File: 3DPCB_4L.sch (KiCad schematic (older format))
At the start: 186 parts, among them IC1 DRV8825, IC2 DRV8825, IC3 DRV8825, IC4 DRV8825, IC5 DRV8825, IC6 MP9943, J10 , J11 , J12 , J13 , J14 , J15 , J16 , J2 , J3 , J4 , J5 , J6 , J7 , J8 , J9 , K1 CONN_3, K2 CONN_3, K3 CONN_3, K4 CONN_3, K5 CONN_3, K6 CONN_3, K7 CONN_3, K8 CONN_3, K9 CONN_3, P1 CONN_8, P11 CONN_3X2, P12 CONN_3X2, P13 CONN_4, P2 CONN_8, P5 CONN_4, P6 CONN_4, P7 CONN_4, P8 CONN_02X03, P9 CONN_4, U1 CONN_4_LERCHE, U10 MICRO-SD, U11 TC4427, U12 MCP4728, U13 CONN_4_LERCHE, U15 SPST_MOMENTARY, U16 CONN_4_LERCHE, U2 SPST_MOMENTARY, U21 CONN_4_LERCHE, U22 CONN_4_LERCHE, U23 MCP4728, U24 IRFH5302, U25 CONN_4_LERCHE, U3 BSS84, U4 CONN_4_LERCHE, U5 IRFH5302, U6 LPC1768_TQFP100, U7 IRFH5302, U8 IRFH5302, U9 TC4427

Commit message: Minor changes DONT USE NOW
Do not use this right now, changes are still coming in.
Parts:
- L2: value IHLP1212-10uH -> IHLP1212BZER2R2M11
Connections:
- net labels added: P2.11
- net labels removed: SD_CD
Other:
- note added: "Filter-caps placed closely to LPC1769"
- note added: "Todo: Change so external Ethernet-board is \npossible to add. 18-11-2016"
- moved on the sheet: C49, D10, R17, R41, R42, R43, U10

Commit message: Branching to follow Smoothieboard V1.1
Update, following Smoothieboard V1.1
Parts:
- added U?: A5984_LP, symbol A5984_LP
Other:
- moved on the sheet: C22, C23, C24, C25, C26, C27, C28, C29, C30, C31, C70, C71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

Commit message: Added A5984 to schematic
Added A5984 to schematic
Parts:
- removed C35, C40, C41, C42, C68: 470n, LercheTech:Lerche_C0603, symbol C-RESCUE-3DPCB_4L
- removed IC1, IC2, IC3, IC4, IC5: DRV8825, LercheTech:Lerche_TSSOP28_EP, symbol DRV8825
- added IC1, IC2, IC3, IC4: A5984_LP, LercheTech:Lerche_TSSOP24_EP, symbol A5984_LP
- C36, C37, C8: value 10n -> 100nF
- C67: value 10n -> 100n
- IC5: renamed from U?; footprint (none) -> LercheTech:Lerche_TSSOP24_EP
- R21, R22, R23, R24, R29, R30, R31, R32, R33, R37: value 0R1 -> 0R05
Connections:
- net labels removed: ~FAULT1, ~FAULT2, ~FAULT3, ~FAULT4, ~FAULT5, ~HOME1, ~HOME2, ~HOME3, ~HOME4, ~HOME5
- wire segments 446 -> 477
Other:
- moved on the sheet: C22, C23, C24, C25, C26, C27, C28, C29, C30, C31, C32, C33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

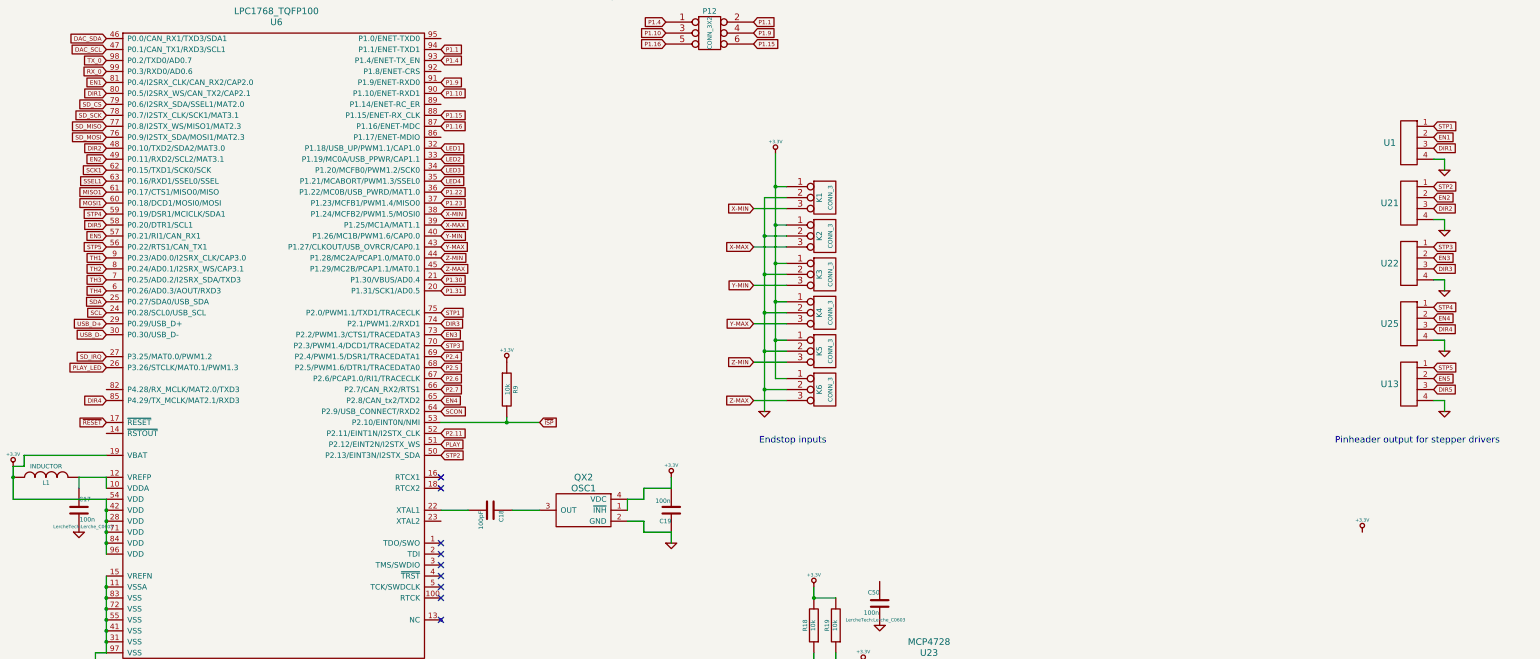
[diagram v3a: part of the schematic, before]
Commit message: First A5984 in place - DO NOT USE
First A5984 in place - DO NOT USE
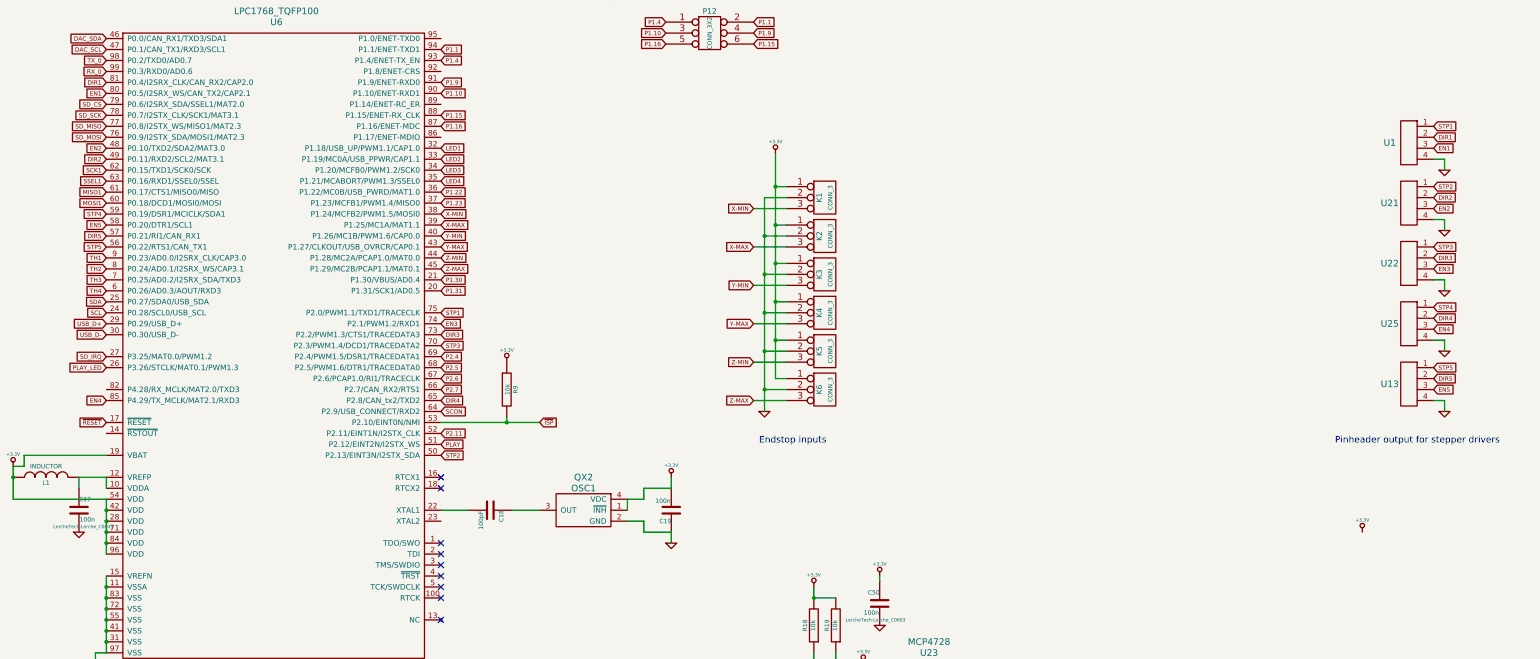
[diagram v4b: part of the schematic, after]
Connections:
- net +3.3V: now also C50.1
- net DIR1: now also U1.2, U6.81 (P0.4/I2SRX_CLK/CAN_RX2/CAP2.0); no longer U1.3, U6.80 (P0.5/I2SRX_WS/CAN_TX2/CAP2.1)
- net DIR2: now also U21.2, U6.49 (P0.11/RXD2/SCL2/MAT3.1); no longer U21.3, U6.48 (P0.10/TXD2/SDA2/MAT3.0)
- net DIR3: now also U22.2, U6.73 (P2.2/PWM1.3/CTS1/TRACEDATA3); no longer U22.3, U6.74 (P2.1/PWM1.2/RXD1)
- net DIR4: now also U25.2, U6.65 (P2.8/CAN_tx2/TXD2); no longer U25.3, U6.85 (P4.29/TX_MCLK/MAT2.1/RXD3)
- net DIR5: now also U13.2, U6.57 (P0.21/RI1/CAN_RX1); no longer U13.3, U6.58 (P0.20/DTR1/SCL1)
- net EN1: now also U1.3, U6.80 (P0.5/I2SRX_WS/CAN_TX2/CAP2.1); no longer U1.2, U6.81 (P0.4/I2SRX_CLK/CAN_RX2/CAP2.0)
- net EN2: now also U21.3, U6.48 (P0.10/TXD2/SDA2/MAT3.0); no longer U21.2, U6.49 (P0.11/RXD2/SCL2/MAT3.1)
- net EN3: now also U22.3, U6.74 (P2.1/PWM1.2/RXD1); no longer U22.2, U6.73 (P2.2/PWM1.3/CTS1/TRACEDATA3)
- net EN4: now also U25.3, U6.85 (P4.29/TX_MCLK/MAT2.1/RXD3); no longer U25.2, U6.65 (P2.8/CAN_tx2/TXD2)
- net EN5: now also U13.3, U6.58 (P0.20/DTR1/SCL1); no longer U13.2, U6.57 (P0.21/RI1/CAN_RX1)

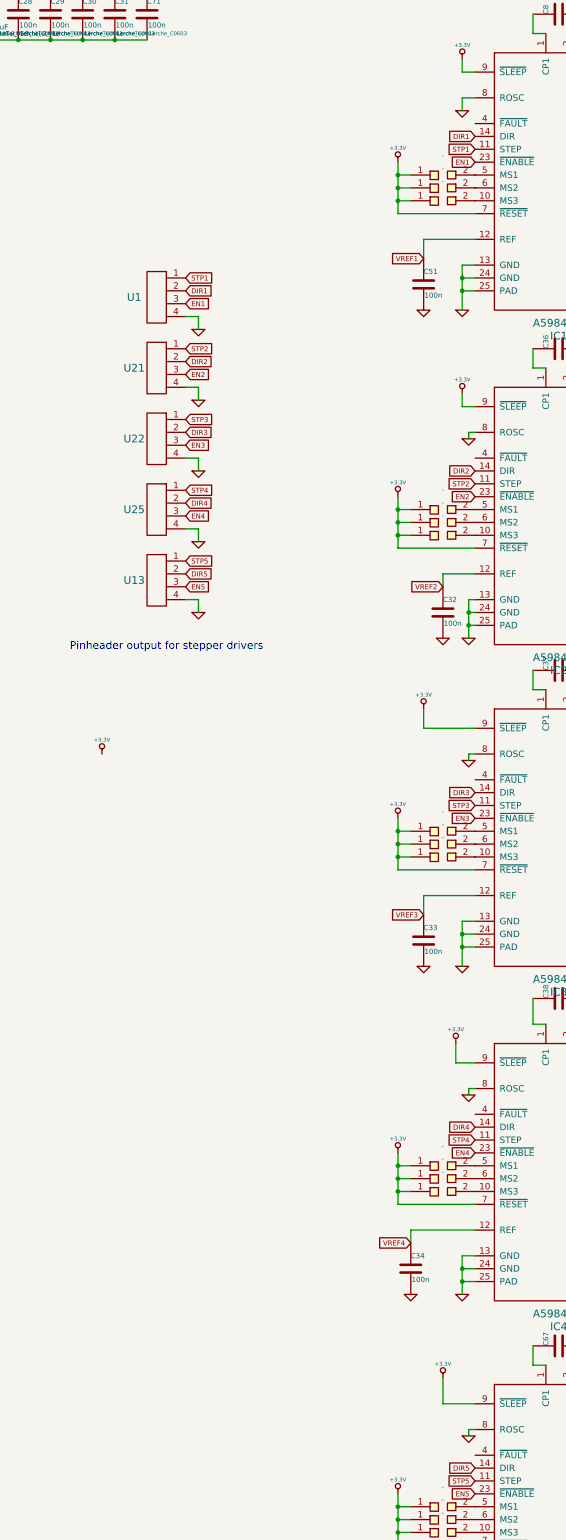
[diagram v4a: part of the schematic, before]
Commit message: Adding resistor to ROSC - DONT USE
DONT USE YET
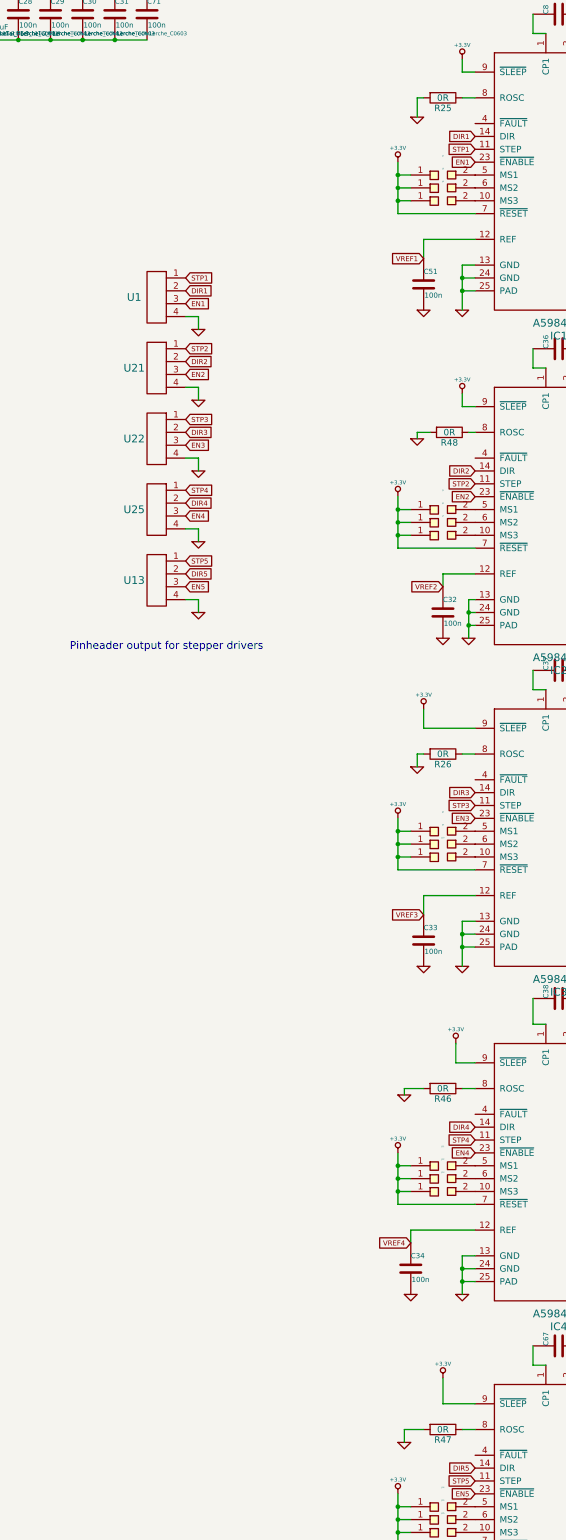
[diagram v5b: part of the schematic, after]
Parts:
- added R25, R26, R46, R47, R48: 0R, LercheTech:Lerche_R0603, symbol R
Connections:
- net GND: now also R25.2, R26.2, R46.2, R47.2, R48.2; no longer IC1.8 (ROSC), IC2.8 (ROSC), IC3.8 (ROSC), IC4.8 (ROSC), IC5.8 (ROSC)
- new net: IC5.8 (ROSC), R47.1
- new net: IC4.8 (ROSC), R46.1
- new net: IC3.8 (ROSC), R26.1
- new net: IC2.8 (ROSC), R48.1
- new net: IC1.8 (ROSC), R25.1

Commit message: Added smaller parts
Added LEDs to MOSFETs, adding AVCC and AGND connector
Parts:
- added C35: 100n, LercheTech:Lerche_C0603, symbol C-RESCUE-3DPCB_4L
- added D11, D12, D13, D14: LED, LEDs:LED_0603, symbol LED-RESCUE-3DPCB_4L
- added P3: CONN_01X02, Pin_Headers:Pin_Header_Straight_1x02_Pitch2.54mm, symbol CONN_01X02
- added R49, R50, R51, R52: 4k7, LercheTech:Lerche_R0603, symbol R-RESCUE-3DPCB_4L
- P8: footprint (none) -> LercheTech:Lerche_Molex_Microfit_0430450607
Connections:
- net GND: now also C35.2, D11.2 (K), D12.2 (K), D13.2 (K), D14.2 (K), P3.2 (P2)
- net at C17.1, L1.2, U6.10 (VDDA)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: now also C35.1, P3.1 (P1)
- net at R14.1, R56.2, U5.1 (G): now also R49.1
- net at R15.1, R58.2, U7.1 (G): now also R50.1
- net at R16.1, R57.2, U8.1 (G): now also R51.1
- net at R20.1, R59.2, U24.1 (G): now also R52.1
- new net: D13.1 (A), R49.2
- new net: D14.1 (A), R51.2
- new net: D11.1 (A), R50.2
- new net: D12.1 (A), R52.2
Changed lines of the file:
@@
 F 0 "C17" H 5450 6800 40  0000 L CNN
 F 1 "100n" H 5456 6615 40  0000 L CNN
-F 2 "LercheTech:Lerche_C0603" H 5488 6550 30  0000 C CNN
+F 2 "LercheTech:Lerche_C0603" H 5488 6550 30  0001 C CNN
 F 3 "~" H 5450 6700 60  0000 C CNN
 	1    5450 6700
@@
 Connection ~ 4850 6400
 Wire Wire Line
-	5450 6400 5450 6500
+	5450 5900 5450 6500
 Wire Wire Line
 	3400 1850 4300 1850
@@
 	10950 11050 11150 11050
 Wire Wire Line
-	11050 11150 11050 11050
+	11050 10500 11050 11150
 Connection ~ 11050 11050
 Wire Wire Line
@@
 	13600 11050 13800 11050
 Wire Wire Line
-	13700 11150 13700 11050
+	13700 10450 13700 11150
 Connection ~ 13700 11050
 Wire Wire Line
 	13600 12300 13800 12300
 Wire Wire Line
-	13700 12400 13700 12300
+	13700 11950 13700 12400
 Connection ~ 13700 12300
 Wire Wire Line
-	11050 12400 11050 12300
+	11050 11950 11050 12400
 Wire Wire Line
 	10950 12300 11150 12300
@@
 Text Notes 12200 9750 0    60   ~ 0
 DAC's for stepper current control
-Text Notes 11250 10450 0    60   ~ 0
+Text Notes 11200 10150 0    60   ~ 0
 MOSFET outputs
 Text Notes 4100 10500 0    60   ~ 0
@@
 $EndComp
 Wire Wire Line
-	9850 11200 10700 11200
+	9850 11450 9850 11750
 Wire Wire Line
-	10700 11200 10700 11750
-Wire Wire Line
-	10700 11750 13000 11750
+	9850 11750 13000 11750
 Wire Wire Line
 	13000 11750 13000 11050
 Wire Wire Line
-	9850 12450 10250 12450
-Wire Wire Line
-	10250 12450 10250 13150
+	9850 12750 9850 13150
 Wire Wire Line
-	10250 13150 13000 13150
+	9850 13150 13000 13150
 Wire Wire Line
 	13000 13150 13000 12300
@@
 Wire Wire Line
 	9850 11050 9850 10650
-Wire Wire Line
-	9850 10650 9550 10650
-Wire Wire Line
-	9850 11200 9850 11450
-Wire Wire Line
-	9850 11450 9550 11450
 $Comp
 L C C49
@@
 $EndComp
 Wire Wire Line
-	9850 12450 9850 12750
-Wire Wire Line
-	9850 12750 9550 12750
-Wire Wire Line
 	9850 12300 9850 12000
-Wire Wire Line
-	9850 12000 9550 12000
 Text GLabel 9050 9650 0    39   Input ~ 0
 MOSVCC
@@
 F 0 "P8" H 1400 4500 50  0000 C CNN
 F 1 "CONN_02X03" H 1400 4100 50  0000 C CNN
-F 2 "" H 1400 3100 50  0000 C CNN
+F 2 "LercheTech:Lerche_Molex_Microfit_0430450607" H 1400 3100 50  0001 C CNN
 F 3 "" H 1400 3100 50  0000 C CNN
 	1    1400 4300
@@
 $EndComp
 Wire Wire Line
-	20050 3300 19950 3300
+	19950 3300 20050 3300
 Wire Wire Line
 	19950 3100 19950 3450
@@
 $EndComp
 Wire Wire Line
-	20050 2700 19450 2700
+	19450 2700 20050 2700
 Wire Wire Line
-	19450 2700 19450 2300
+	19450 2300 19450 2700
 Wire Wire Line
 	19550 2600 19450 2600
@@
 Wire Wire Line
 	19500 12150 19500 12250
+$Comp
+L CONN_01X02 P3
+U 1 1 58779D11
+P 4300 5950
+F 0 "P3" H 4300 6100 50  0000 C CNN
+F 1 "CONN_01X02" V 4400 5950 50  0000 C CNN
+F 2 "Pin_Headers:Pin_Header_Straight_1x02_Pitch2.54mm" H 4300 5950 50  0001 C CNN
+F 3 "" H 4300 5950 50  0000 C CNN
+	1    4300 5950
+	-1   0    0    -1
+$EndComp
+Connection ~ 5450 6400
+Wire Wire Line
+	5450 5900 4500 5900
+$Comp
+L GND-RESCUE-3DPCB_4L #PWR0131
+U 1 1 5877C07D
+P 4600 6100
+F 0 "#PWR0131" H 4600 6100 30  0001 C CNN
+F 1 "GND" H 4600 6030 30  0001 C CNN
+F 2 "" H 4600 6100 60  0000 C CNN
+F 3 "" H 4600 6100 60  0000 C CNN
+	1    4600 6100
+	1    0    0    -1
+$EndComp
+Wire Wire Line
+	4500 6000 4600 6000
+Wire Wire Line
+	4600 5750 4600 6100
+$Comp
+L R-RESCUE-3DPCB_4L R49
+U 1 1 5879127B
+P 11300 10500
+F 0 "R49" V 11380 10500 40  0000 C CNN
+F 1 "4k7" V 11307 10501 40  0000 C CNN
+F 2 "LercheTech:Lerche_R0603" V 11230 10500 30  0001 C CNN
+F 3 "~" H 11300 10500 30  0000 C CNN
+	1    11300 10500
+	0    -1   -1   0
+$EndComp
+$Comp
+L LED-RESCUE-3DPCB_4L D13
+U 1 1 587971F1
+P 11850 10500
+F 0 "D13" H 11850 10600 50  0000 C CNN
+F 1 "LED" H 11850 10400 50  0000 C CNN
+F 2 "LEDs:LED_0603" H 11850 10500 60  0001 C CNN
+F 3 "~" H 11850 10500 60  0000 C CNN
+	1    11850 10500
+	1    0    0    -1
+$EndComp
+Wire Wire Line
+	11650 10500 11550 10500
+$Comp
+L GND-RESCUE-3DPCB_4L #PWR0132
+U 1 1 5879B521
+P 12050 10500
+F 0 "#PWR0132" H 12050 10500 30  0001 C CNN
+F 1 "GND" H 12050 10430 30  0001 C CNN
+F 2 "" H 12050 10500 60  0000 C CNN
+F 3 "" H 12050 10500 60  0000 C CNN
+	1    12050 10500
+	0    -1   -1   0
+$EndComp
+$Comp
+L R-RESCUE-3DPCB_4L R51
+U 1 1 5879B769
+P 11300 11950
+F 0 "R51" V 11380 11950 40  0000 C CNN
+F 1 "4k7" V 11307 11951 40  0000 C CNN
+F 2 "LercheTech:Lerche_R0603" V 11230 11950 30  0001 C CNN
+F 3 "~" H 11300 11950 30  0000 C CNN
+	1    11300 11950
+	0    -1   -1   0
+$EndComp
+$Comp
+L LED-RESCUE-3DPCB_4L D14
+U 1 1 5879BFF3
+P 11850 11950
+F 0 "D14" H 11850 12050 50  0000 C CNN
+F 1 "LED" H 11850 11850 50  0000 C CNN
+F 2 "LEDs:LED_0603" H 11850 11950 60  0001 C CNN
+F 3 "~" H 11850 11950 60  0000 C CNN
+	1    11850 11950
+	1    0    0    -1
+$EndComp
+$Comp
+L GND-RESCUE-3DPCB_4L #PWR0133
+U 1 1 5879C507
+P 12050 11950
+F 0 "#PWR0133" H 12050 11950 30  0001 C CNN
+F 1 "GND" H 12050 11880 30  0001 C CNN
+F 2 "" H 12050 11950 60  0000 C CNN
+F 3 "" H 12050 11950 60  0000 C CNN
+	1    12050 11950
+	0    -1   -1   0
+$EndComp
+Wire Wire Line
+	11650 11950 11550 11950
+$Comp
+L R-RESCUE-3DPCB_4L R50
+U 1 1 5879F744
+P 13950 10450
+F 0 "R50" V 14030 10450 40  0000 C CNN
+F 1 "4k7" V 13957 10451 40  0000 C CNN
+F 2 "LercheTech:Lerche_R0603" V 13880 10450 30  0001 C CNN
+F 3 "~" H 13950 10450 30  0000 C CNN
+	1    13950 10450
+	0    -1   -1   0
+$EndComp
+$Comp
+L LED-RESCUE-3DPCB_4L D11
+U 1 1 5879F9AC
+P 14400 10450
+F 0 "D11" H 14400 10550 50  0000 C CNN
+F 1 "LED" H 14400 10350 50  0000 C CNN
+F 2 "LEDs:LED_0603" H 14400 10450 60  0001 C CNN
+F 3 "~" H 14400 10450 60  0000 C CNN
+	1    14400 10450
+	1    0    0    -1
+$EndComp
+$Comp
+L GND-RESCUE-3DPCB_4L #PWR0134
+U 1 1 5879FC1F
+P 14650 10550
+F 0 "#PWR0134" H 14650 10550 30  0001 C CNN
+F 1 "GND" H 14650 10480 30  0001 C CNN
+F 2 "" H 14650 10550 60  0000 C CNN
+F 3 "" H 14650 10550 60  0000 C CNN
+	1    14650 10550
+	1    0    0    -1
+$EndComp
+Wire Wire Line
+	14600 10450 14650 10450
+Wire Wire Line
+	14650 10450 14650 10550
+$Comp
+L R-RESCUE-3DPCB_4L R52
+U 1 1 587A1BB4
+P 13950 11950
+F 0 "R52" V 14030 11950 40  0000 C CNN
+F 1 "4k7" V 13957 11951 40  0000 C CNN
+F 2 "LercheTech:Lerche_R0603" V 13880 11950 30  0001 C CNN
+F 3 "~" H 13950 11950 30  0000 C CNN
+	1    13950 11950
+	0    -1   -1   0
+$EndComp
+$Comp
+L LED-RESCUE-3DPCB_4L D12
+U 1 1 587A1E30
+P 14400 11950
+F 0 "D12" H 14400 12050 50  0000 C CNN
+F 1 "LED" H 14400 11850 50  0000 C CNN
+F 2 "LEDs:LED_0603" H 14400 11950 60  0001 C CNN
+F 3 "~" H 14400 11950 60  0000 C CNN
+	1    14400 11950
+	1    0    0    -1
+$EndComp
+$Comp
+L GND-RESCUE-3DPCB_4L #PWR0135
+U 1 1 587A20AD
+P 14650 12050
+F 0 "#PWR0135" H 14650 12050 30  0001 C CNN
+F 1 "GND" H 14650 11980 30  0001 C CNN
+F 2 "" H 14650 12050 60  0000 C CNN
+F 3 "" H 14650 12050 60  0000 C CNN
+	1    14650 12050
+	1    0    0    -1
+$EndComp
+Wire Wire Line
+	14600 11950 14650 11950
+Wire Wire Line
+	14650 11950 14650 12050
+Wire Wire Line
+	9850 10650 9550 10650
+Wire Wire Line
+	9850 12750 9550 12750
+Wire Wire Line
+	9850 12000 9550 12000
+Wire Wire Line
+	9850 11450 9550 11450
+$Comp
+L C-RESCUE-3DPCB_4L C35
+U 1 1 587D374F
+P 4800 5750
+F 0 "C35" H 4800 5850 40  0000 L CNN
+F 1 "100n" H 4806 5665 40  0000 L CNN
+F 2 "LercheTech:Lerche_C0603" H 4838 5600 30  0001 C CNN
+F 3 "~" H 4800 5750 60  0000 C CNN
+	1    4800 5750
+	0    1    1    0
+$EndComp
+Connection ~ 4600 6000
+Wire Wire Line
+	5000 5750 5000 5900
+Connection ~ 5000 5900
 $EndSCHEMATC
